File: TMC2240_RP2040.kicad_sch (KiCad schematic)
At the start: 38 parts, among them J10 Screw_Terminal_01x01, J11 Screw_Terminal_01x01, J12 Screw_Terminal_01x01, J2 LIMIT, J5 Screw_Terminal_01x01, J6 Screw_Terminal_01x01, J7 Screw_Terminal_01x01, J8 Screw_Terminal_01x01, J9 Screw_Terminal_01x01

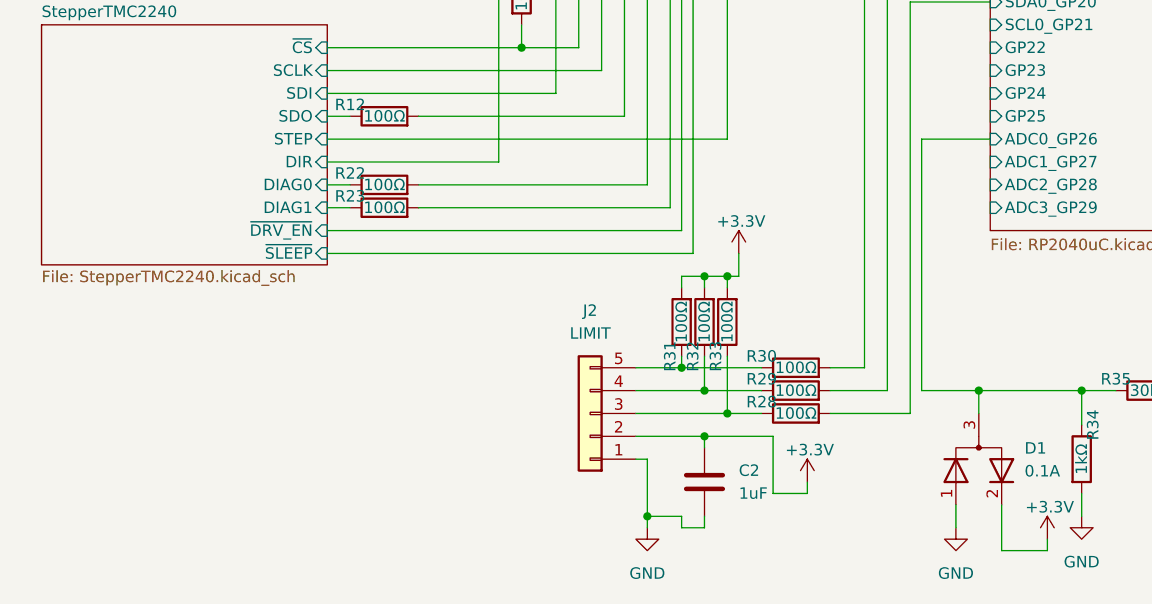
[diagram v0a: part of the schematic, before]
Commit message: Added an ADC input pin, and protection diodes. Updated the OV load resistor to 0805. Cleaned up a few silk screen overlaps.
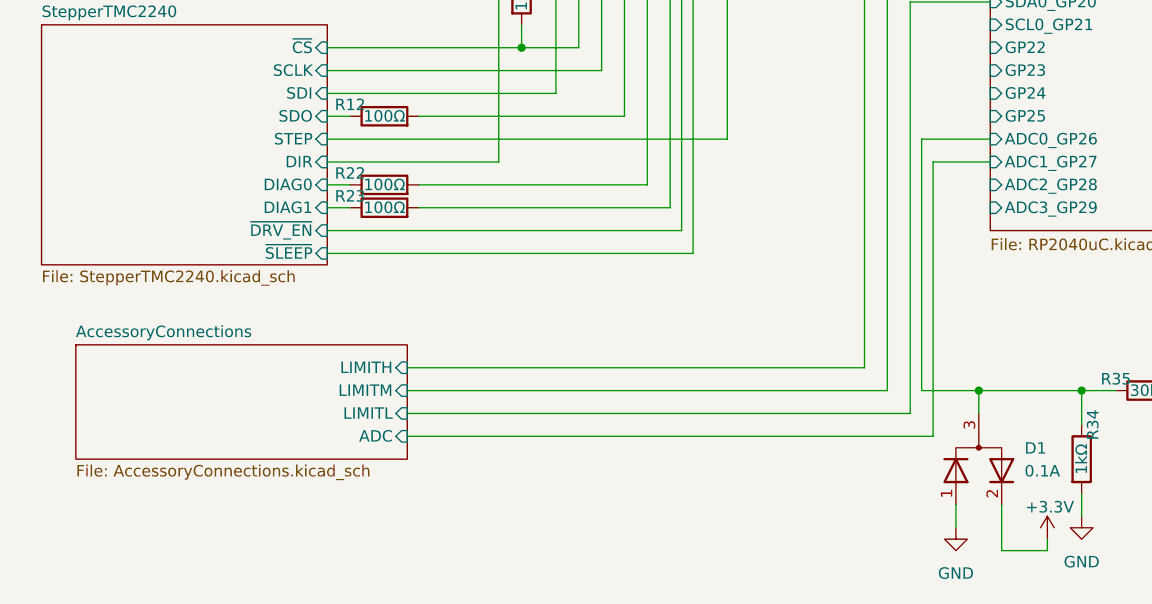
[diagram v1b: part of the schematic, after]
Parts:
- removed C2: 1uF, Capacitor_SMD:C_0603_1608Metric, symbol Device:C
- removed J2: LIMIT, Connector_PinHeader_2.54mm:PinHeader_1x05_P2.54mm_Vertical, symbol Connector_Generic:Conn_01x05
- removed R28, R29, R30, R31, R32, R33: 100Ω, Resistor_SMD:R_0603_1608Metric, symbol Device:R
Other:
- added sheet AccessoryConnections (AccessoryConnections.kicad_sch)
